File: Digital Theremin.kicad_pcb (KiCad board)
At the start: 2 copper layers, 95 x 55 mm, 57 parts, among them J1 Conn_01x02_Female, J2 AudioJack3, J3 USB_B_Micro, J4 Conn_01x03_Female, SW1 SW_Push, SW2 SW_Push, SW3 SW_SPDT, U1 AP2204K-3.0, U2 TDA2822, U3 NE555P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

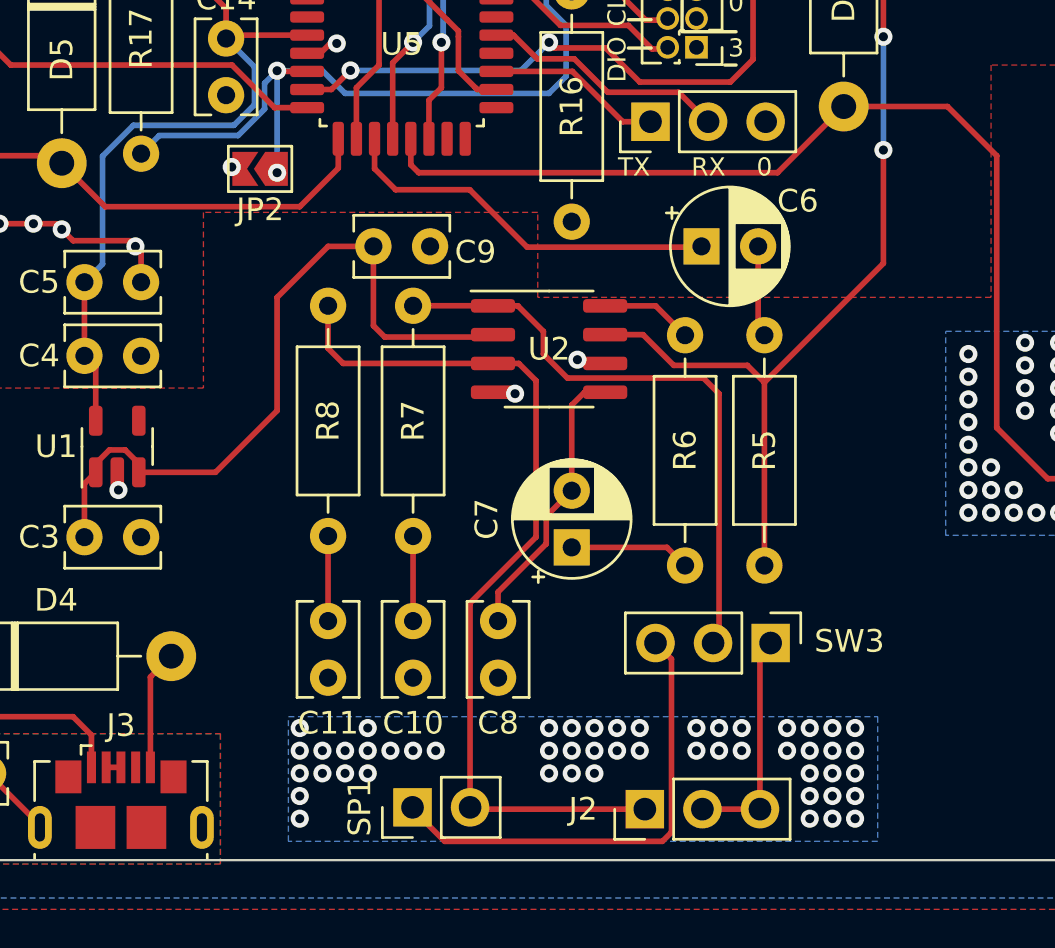
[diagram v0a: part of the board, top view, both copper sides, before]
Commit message: Software. Add filter cap
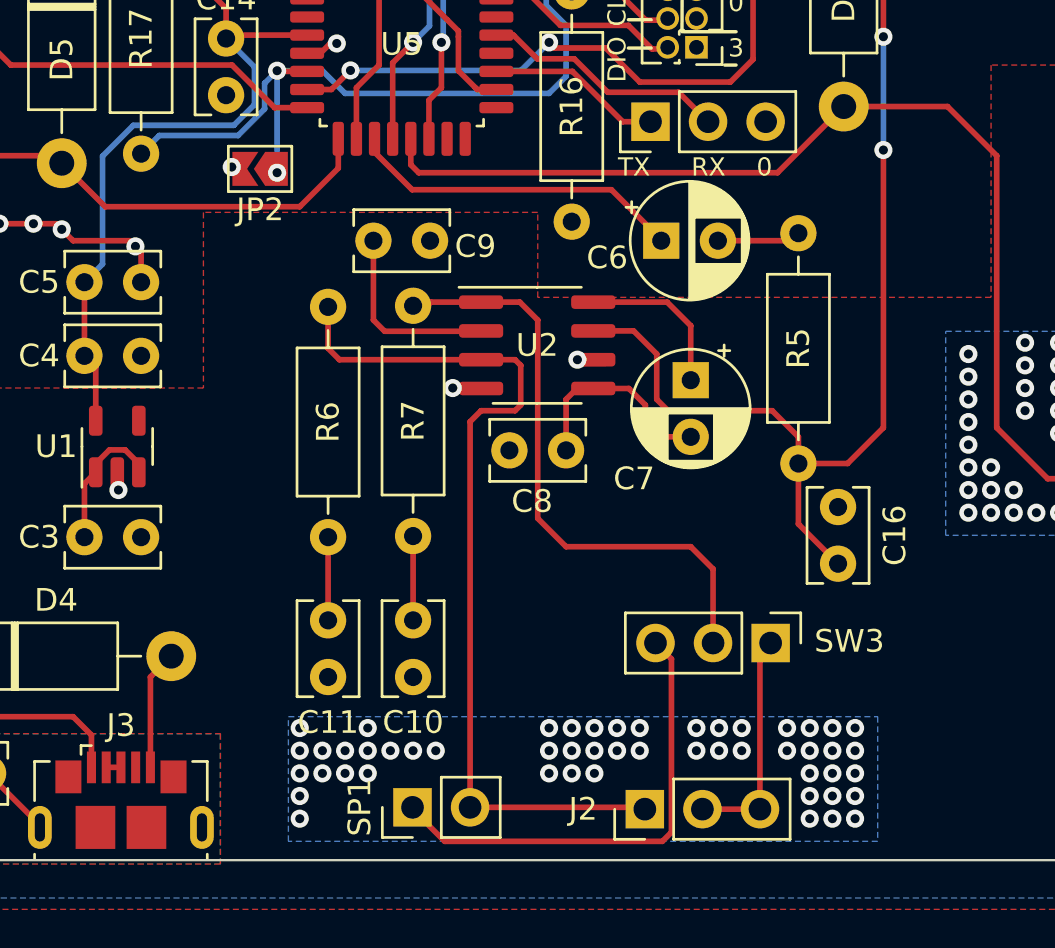
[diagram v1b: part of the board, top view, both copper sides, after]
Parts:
- removed R8: 4.7, Resistor_THT:R_Axial_DIN0207_L6.3mm_D2.5mm_P10.16mm_Horizontal
- added C16: .1u, Capacitor_THT:C_Rect_L4.0mm_W2.5mm_P2.50mm, F.Cu at (149.8, 101.2)
- C10, C11: value 100n -> .1u
- C6: value 22u -> 100u
- C7: value 10u -> 100u
- R5: value 120k -> 510k
- R6: value 3.9k -> 4.7
- moved R6 15.8 mm to (127.2, 102.6)
- moved C8 10.0 mm to (135.2, 98.8), turned to 0 degrees
- moved C7 9.05 mm to (143.2, 95.7), turned to -90 degrees
- moved R5 4.74 mm to (148.0, 99.3)
- moved C6 1.79 mm to (141.9, 89.5)
- moved U2 0.55 mm to (136.5, 94.1)
- moved C9 0.25 mm to (129.2, 89.5)
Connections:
- R6 pad 1: Net-(C7-Pad1) -> Net-(C11-Pad2)
- R6 pad 2: Net-(R6-Pad2) -> /Output Low
- U2 pad 8: Net-(R6-Pad2) -> Net-(C7-Pad1)
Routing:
- net +5V: track 74.4 -> 56.4 mm
- net Net-(R5-Pad1): track 49.8 -> 57.3 mm
- net Net-(R6-Pad2): track 4.06 -> 0.00 mm
- net Net-(C7-Pad2): track 12.6 -> 9.42 mm
- net /MCU Audio Out: track 17.2 -> 14.9 mm
- net Net-(C7-Pad1): track 5.33 -> 7.13 mm

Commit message: Software
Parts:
- moved C9 4.37 mm to (131.0, 93.5), turned to -90 degrees
- moved C10 3.51 mm to (127.8, 107.4)
- moved R7 3.51 mm to (127.8, 101.2)
- moved C11 3.05 mm to (124.5, 107.4)
- moved R6 3.05 mm to (124.5, 101.2)
- moved R16 0.71 mm to (138.5, 79.0)
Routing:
- net +5V: track 56.4 -> 50.9 mm
- net Net-(R7-Pad2): track 26.6 -> 30.2 mm
- net /Output Low: track 39.7 -> 43.2 mm
- net /MCU Audio Out: track 14.9 -> 17.5 mm
- net /Volume Frequency: track 49.1 -> 47.4 mm
- net Net-(C7-Pad2): track 9.42 -> 8.83 mm
- net GND: vias 9 -> 20
- net +3V0: vias 0 -> 24
- added copper zone on B.Cu, net +3V0

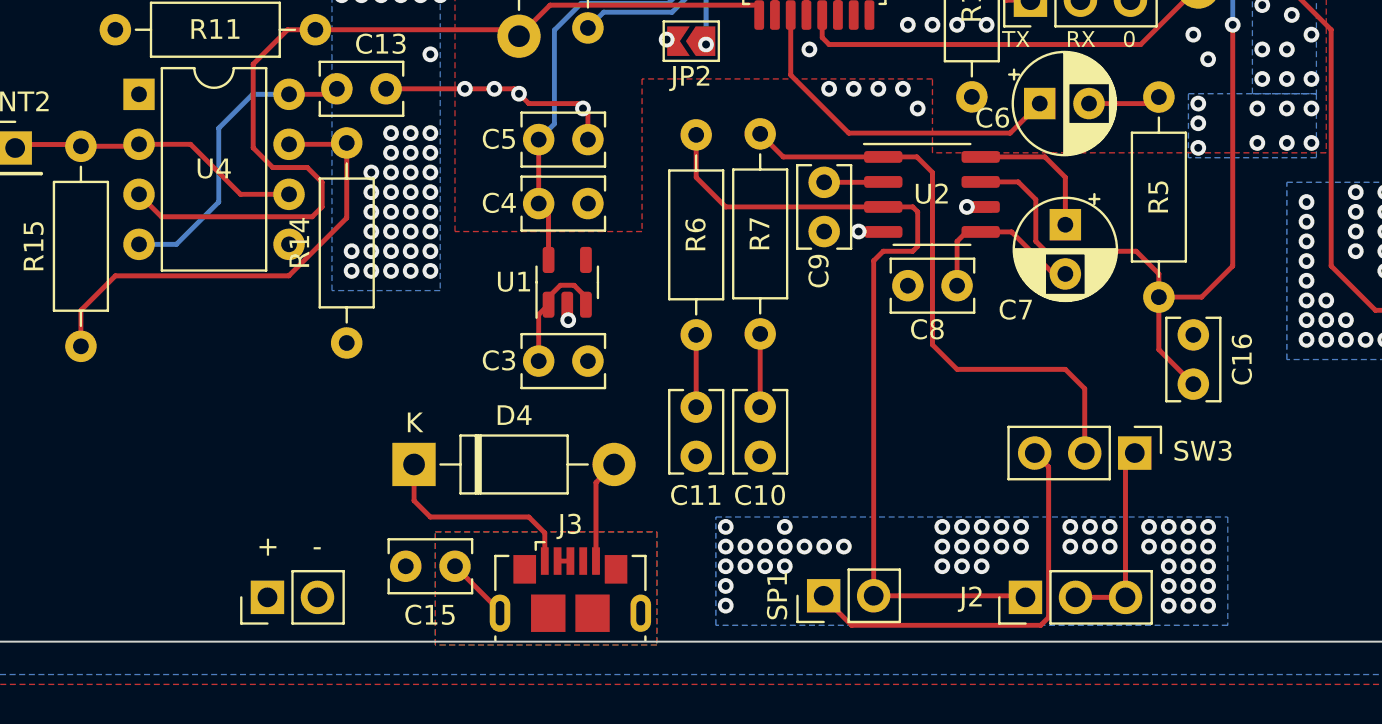
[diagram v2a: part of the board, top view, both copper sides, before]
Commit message: Single ended layout
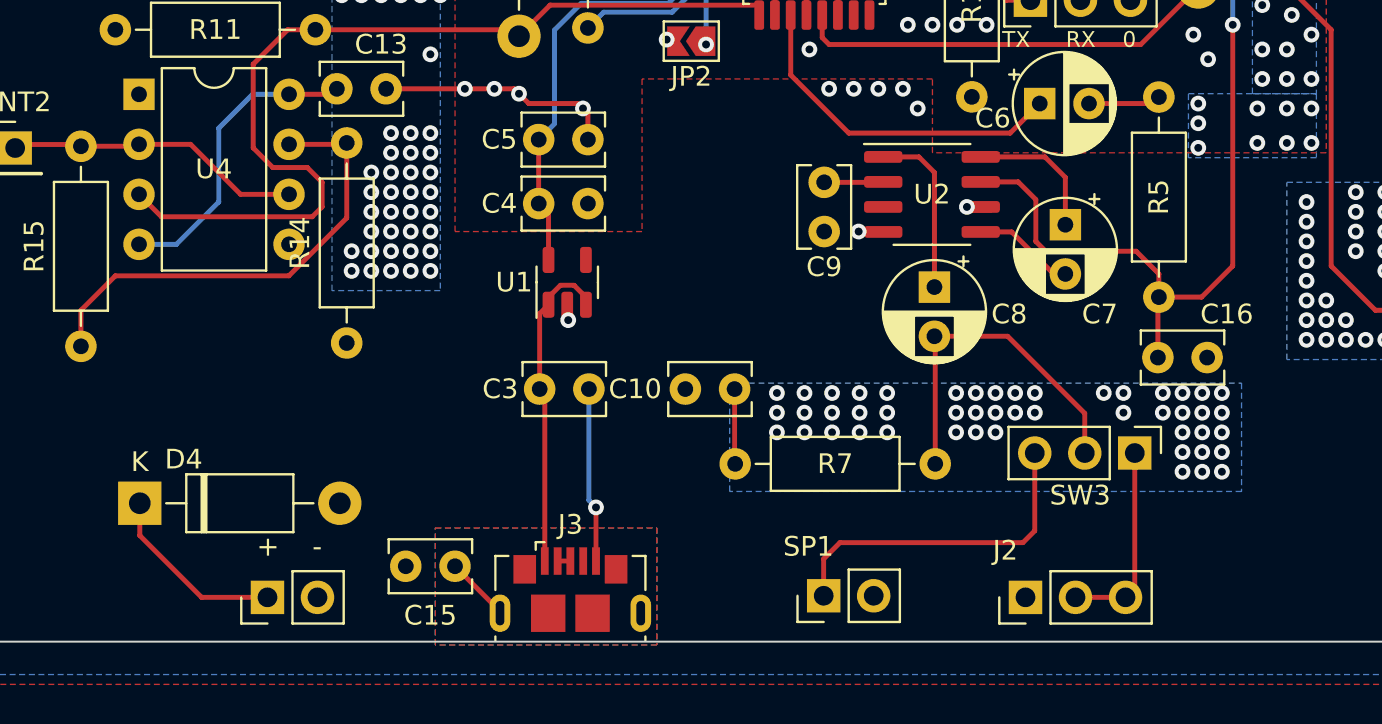
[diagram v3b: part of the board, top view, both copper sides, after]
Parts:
- removed C11: .1u, Capacitor_THT:C_Rect_L4.0mm_W2.5mm_P2.50mm
- removed R6: 4.7, Resistor_THT:R_Axial_DIN0207_L6.3mm_D2.5mm_P10.16mm_Horizontal
- C16: value .1u -> DNF
- C8: value 10n -> 470u; footprint Capacitor_THT:C_Rect_L4.0mm_W2.5mm_P2.50mm -> Capacitor_THT:CP_Radial_D5.0mm_P2.50mm
- moved D4 14.1 mm to (96.2, 109.8)
- moved R7 6.72 mm to (126.5, 107.8), turned to 0 degrees
- moved C10 5.11 mm to (124.0, 104.0), turned to 0 degrees
- moved C3 1.42 mm to (116.5, 104.0)
- moved C8 1.35 mm to (136.6, 98.8), turned to -90 degrees
- moved C16 1.35 mm to (150.4, 102.4), turned to 180 degrees
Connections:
- C7 pad 2: Net-(C7-Pad2) -> GND
- C8 pad 1: GND -> Net-(U2-Pad1)
- C8 pad 2: Net-(C7-Pad2) -> Net-(R7-Pad2)
- J2 pad 1: /Output Low -> GND
- SP1 pad 2: /Output Low -> GND
- U2 pad 1: Net-(R7-Pad2) -> Net-(U2-Pad1)
- U2 pad 3: /Output Low -> unconnected-(U2-Pad3)
- U2 pad 5: Net-(C7-Pad2) -> GND
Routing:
- net /Output Low: track 43.2 -> 0.00 mm
- net Net-(R7-Pad2): track 30.2 -> 17.8 mm
- net +5V: track 50.9 -> 60.0 mm, vias 126 -> 123
- net Net-(C7-Pad2): track 8.83 -> 0.00 mm
- net GND: track 22.8 -> 31.6 mm, vias 20 -> 21
- net Net-(U2-Pad1): track 0.00 -> 8.75 mm
- net /Speaker: track 20.8 -> 17.1 mm
- net Net-(C11-Pad2): track 3.67 -> 0.00 mm
- net Net-(C16-Pad2): track 57.4 -> 55.3 mm

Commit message: Antenna mounts
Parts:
- ANT1, ANT2: footprint Connector_PinHeader_2.54mm:PinHeader_1x01_P2.54mm_Vertical -> MountingHole:MountingHole_3.2mm_M3_Pad_Via
- J2: value AudioJack3 -> AudioJack3_Dual_Switch; footprint Connector_PinHeader_2.54mm:PinHeader_1x03_P2.54mm_Vertical -> Connector_Audio:Jack_3.5mm_CUI_SJ1-3525N_Horizontal
- moved ANT1 11.8 mm to (182.0, 105.8)
- moved J2 11.1 mm to (150.8, 120.3), turned to 0 degrees
- moved D4 8.74 mm to (93.8, 118.2)
- moved J1 8.74 mm to (100.3, 123.0)
- moved ANT2 8.69 mm to (94.2, 84.2)
- moved C15 8.22 mm to (115.0, 120.8)
- moved J3 8.22 mm to (120.9, 121.9)
- moved SW2 6.43 mm to (170.2, 64.7)
- moved R11 5.18 mm to (97.8, 90.1)
- moved SW1 4.61 mm to (99.2, 64.7)
- moved C13 4.43 mm to (107.0, 93.1)
- moved R14 4.43 mm to (107.5, 106.0)
- moved R15 4.43 mm to (94.0, 106.2)
- moved U4 4.43 mm to (97.0, 93.4)
- moved C12 4.00 mm to (168.5, 97.0)
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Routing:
- net +3V0: track 38.8 -> 75.1 mm, vias 24 -> 30
- net /Output: track 10.1 -> 21.9 mm
- net /Oscillators/Volume Antenna: track 15.2 -> 23.6 mm
- net /Oscillators/Pitch Antenna: track 15.2 -> 23.4 mm
- net +5V: track 60.0 -> 67.2 mm, vias 123 -> 108
- net GND: track 31.6 -> 38.5 mm, vias 21 -> 20
- net /Pitch Frequency: track 76.9 -> 81.1 mm
- net Net-(C15-Pad1): track 3.33 -> 0.00 mm
- net /Volume Frequency: track 47.4 -> 50.2 mm
- net /Function Button: track 34.5 -> 36.8 mm, vias 0 -> 2
- net Net-(R14-Pad2): track 24.0 -> 25.0 mm
- net /Calibrate Button: track 63.1 -> 62.6 mm
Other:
- board size 95 x 55 mm -> 100 x 63 mm

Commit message: Update
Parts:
- added H1: MountingHole_Pad, MountingHole:MountingHole_3.7mm_Pad, F.Cu at (101.3, 72.3)
- added H2: MountingHole_Pad, MountingHole:MountingHole_3.7mm_Pad, F.Cu at (174.7, 72.3)
- added TP1: TestPoint, TestPoint:TestPoint_Loop_D2.50mm_Drill1.0mm, F.Cu at (185.2, 99.1)
- added TP2: TestPoint, TestPoint:TestPoint_Loop_D2.50mm_Drill1.0mm, F.Cu at (91.4, 90.0)
- J3: footprint Connector_USB:USB_Micro-B_GCT_USB3076-30-A -> Connector_USB:USB_Micro-B_Amphenol_10104110_Horizontal
- moved SW1 53.6 mm to (152.8, 64.8)
- moved C2 48.6 mm to (156.2, 75.0), turned to 90 degrees
- moved RV1 39.7 mm to (100.0, 65.0)
- moved R1 31.7 mm to (107.9, 70.3)
- moved RV2 11.2 mm to (139.0, 64.8)
- moved SW2 7.40 mm to (162.8, 64.8)
- moved R2 6.92 mm to (120.9, 70.3)
- moved R4 6.92 mm to (143.7, 70.3)
- moved D4 6.47 mm to (99.9, 116.0)
- moved C1 2.99 mm to (166.0, 75.0), turned to 90 degrees
- moved D1 0.75 mm to (117.0, 64.2)
- moved D2 0.75 mm to (125.0, 64.2)
- moved D3 0.75 mm to (133.0, 64.2)
- moved J3 0.15 mm to (121.0, 122.0)
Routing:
- net /Function Button: track 36.8 -> 49.2 mm, vias 2 -> 3
- net /Pitch pot: track 33.3 -> 40.5 mm
- net Net-(D3-Pad2): track 5.97 -> 12.1 mm
- net /Calibrate Button: track 62.6 -> 58.5 mm
- net +5V: track 67.2 -> 63.6 mm
- net Net-(C16-Pad2): track 55.3 -> 58.5 mm
- net /Oscillators/Pitch Antenna: track 23.4 -> 26.0 mm
- net /Oscillators/Volume Antenna: track 23.6 -> 25.7 mm
- net +3V0: track 75.1 -> 73.5 mm, vias 30 -> 29
- net /Triangle LED: track 17.5 -> 18.4 mm
- net Net-(D1-Pad2): track 4.48 -> 5.39 mm
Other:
- outline, holes or cut-outs redrawn
- board text added: "David Miall 2023"
- board text added: "JLCJLCJLCJLC"
